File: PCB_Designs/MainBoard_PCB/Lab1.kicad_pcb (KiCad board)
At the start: 2 copper layers, 104.7 x 55.6 mm, 84 parts, among them K1 XLR3, P1 CONN_01X06, P10 CONN_01X01, P11 CONN_01X01, P12 CONN_01X01, P2 USB_B, P3 CONN_02X05, P4 CONN_01X02, P5 CONN_02X05, P6 CONN_02X05, P7 CONN_01X01, P8 CONN_01X01, P9 CONN_01X01, Q1 BSS138, Q2 BSS138, Q3 BSS138, Q4 BSS138, Q5 BSS138, Q6 BSS138, Q7 BSS138, U1 STM32F411RETx, U10 24C16, U2 TRACO_POWER_TEL_2-0511, U3 6N137, U4 6N137, U5 6N137, U6 FT232RL, U7 MAX481CSA, U8 UA78M05IDCY, U9 UA78M33CDCY, Y1 8MHz

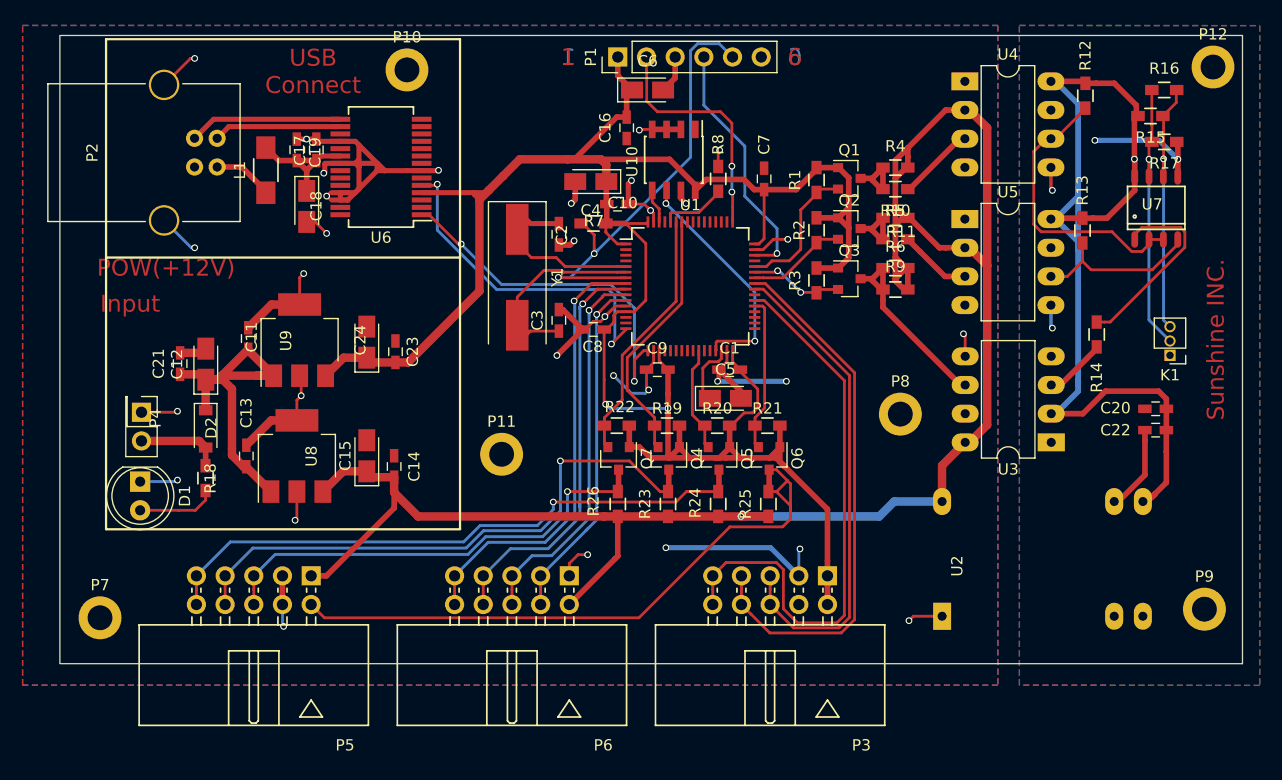
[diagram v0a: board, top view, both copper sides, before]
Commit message: Edited Main_PCB from feedback.
* Added RC-filter (1Mohm, 100nF)
Little cramped now, but whatever.
* Filled out groundplanes a little
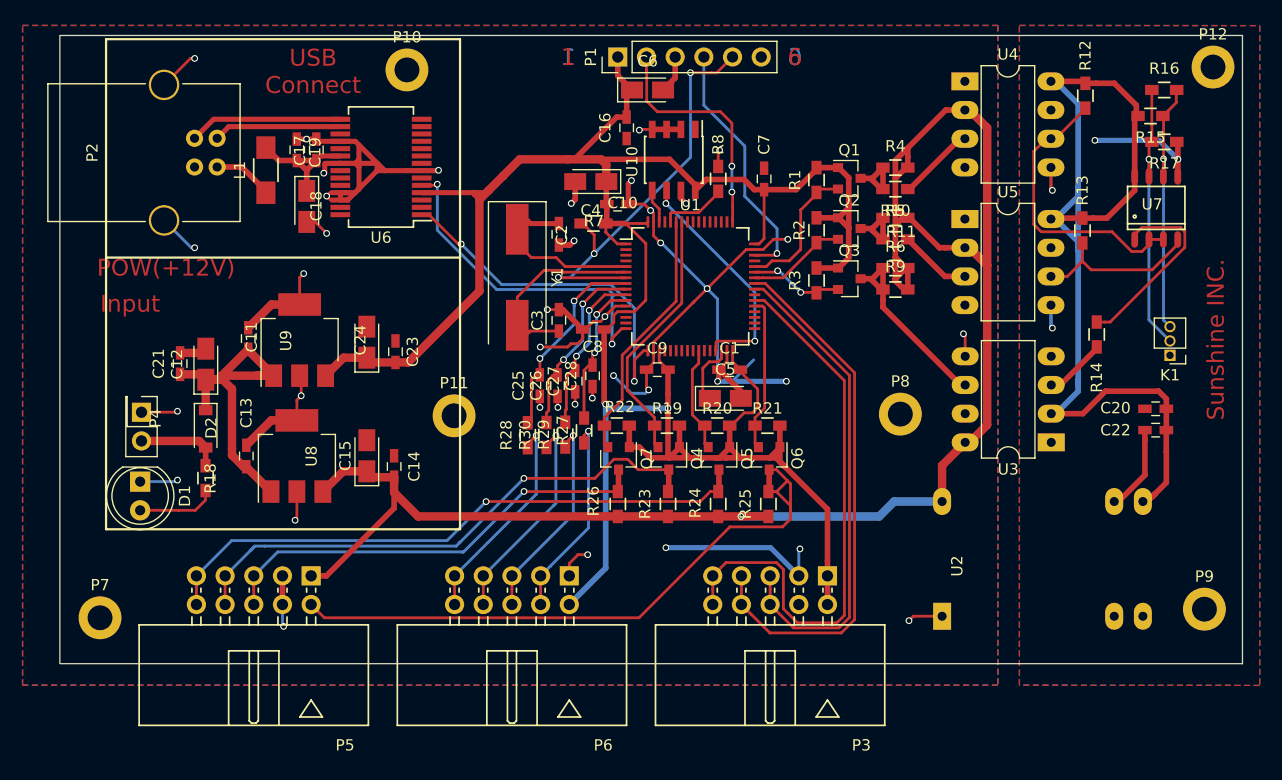
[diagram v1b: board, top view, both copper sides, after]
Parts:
- added C25: 100n, Capacitors_SMD:C_0603_HandSoldering, F.Cu at (77.5, 75.7)
- added C26: 100n, Capacitors_SMD:C_0603_HandSoldering, F.Cu at (79.1, 75.7)
- added C27: 100n, Capacitors_SMD:C_0603_HandSoldering, F.Cu at (80.7, 75.3)
- added C28: 100n, Capacitors_SMD:C_0603_HandSoldering, F.Cu at (82.2, 74.8)
- added R27: 1MEG, Resistors_SMD:R_0603_HandSoldering, F.Cu at (81.5, 79.7)
- added R28: 1MEG, Resistors_SMD:R_0603_HandSoldering, F.Cu at (76.5, 80.1)
- added R29: 1MEG, Resistors_SMD:R_0603_HandSoldering, F.Cu at (79.8, 80.0)
- added R30: 1MEG, Resistors_SMD:R_0603_HandSoldering, F.Cu at (78.1, 80.1)
- moved P11 5.41 mm to (70.0, 78.4)
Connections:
- P1 pad 6: (no net) -> Net-(P1-Pad6)
- P10 pad 1: (no net) -> Net-(P10-Pad1)
- P11 pad 1: (no net) -> Net-(P11-Pad1)
- P12 pad 1: (no net) -> Net-(P12-Pad1)
- P6 pad 2: +5V -> +3V3
- P7 pad 1: (no net) -> Net-(P7-Pad1)
- P8 pad 1: (no net) -> Net-(P8-Pad1)
- P9 pad 1: (no net) -> Net-(P9-Pad1)
- U1 pad 10: Net-(P6-Pad5) -> Net-(C27-Pad2)
- U1 pad 11: Net-(P6-Pad3) -> Net-(C28-Pad2)
- U1 pad 14: (no net) -> Net-(U1-Pad14)
- U1 pad 15: (no net) -> Net-(U1-Pad15)
- U1 pad 2: (no net) -> Net-(U1-Pad2)
- U1 pad 20: (no net) -> Net-(U1-Pad20)
- U1 pad 21: (no net) -> Net-(U1-Pad21)
- U1 pad 22: (no net) -> Net-(U1-Pad22)
- U1 pad 23: (no net) -> Net-(U1-Pad23)
- U1 pad 24: (no net) -> Net-(U1-Pad24)
- U1 pad 25: (no net) -> Net-(U1-Pad25)
- U1 pad 27: (no net) -> Net-(U1-Pad27)
- U1 pad 28: (no net) -> Net-(U1-Pad28)
- U1 pad 3: (no net) -> Net-(U1-Pad3)
- U1 pad 33: (no net) -> Net-(U1-Pad33)
- U1 pad 34: (no net) -> Net-(U1-Pad34)
- U1 pad 35: (no net) -> Net-(U1-Pad35)
- U1 pad 36: (no net) -> Net-(U1-Pad36)
- U1 pad 39: (no net) -> Net-(U1-Pad39)
- U1 pad 4: (no net) -> Net-(U1-Pad4)
- U1 pad 45: (no net) -> Net-(U1-Pad45)
- U1 pad 50: (no net) -> Net-(U1-Pad50)
- U1 pad 51: (no net) -> Net-(U1-Pad51)
- U1 pad 52: (no net) -> Net-(U1-Pad52)
- U1 pad 53: (no net) -> Net-(U1-Pad53)
- U1 pad 54: (no net) -> Net-(U1-Pad54)
- U1 pad 55: (no net) -> Net-(U1-Pad55)
- U1 pad 56: (no net) -> Net-(U1-Pad56)
- U1 pad 57: (no net) -> Net-(U1-Pad57)
- U1 pad 61: (no net) -> Net-(U1-Pad61)
- U1 pad 8: Net-(P6-Pad10) -> Net-(C25-Pad2)
- U1 pad 9: Net-(P6-Pad7) -> Net-(C26-Pad2)
- U10 pad 1: (no net) -> Net-(U10-Pad1)
- U2 pad 7: (no net) -> Net-(U2-Pad7)
- U2 pad 8: (no net) -> Net-(U2-Pad8)
- U3 pad 7: (no net) -> Net-(U3-Pad7)
- U4 pad 7: (no net) -> Net-(U4-Pad7)
- U5 pad 7: (no net) -> Net-(U5-Pad7)
- U6 pad 10: (no net) -> Net-(U6-Pad10)
- U6 pad 11: (no net) -> Net-(U6-Pad11)
- U6 pad 12: (no net) -> Net-(U6-Pad12)
- U6 pad 13: (no net) -> Net-(U6-Pad13)
- U6 pad 14: (no net) -> Net-(U6-Pad14)
- U6 pad 17: (no net) -> Net-(U6-Pad17)
- U6 pad 19: (no net) -> Net-(U6-Pad19)
- U6 pad 2: (no net) -> Net-(U6-Pad2)
- U6 pad 22: (no net) -> Net-(U6-Pad22)
- U6 pad 23: (no net) -> Net-(U6-Pad23)
- U6 pad 27: (no net) -> Net-(U6-Pad27)
- U6 pad 28: (no net) -> Net-(U6-Pad28)
- U6 pad 3: (no net) -> Net-(U6-Pad3)
- U6 pad 6: (no net) -> Net-(U6-Pad6)
- U6 pad 9: (no net) -> Net-(U6-Pad9)
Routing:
- net GND: track 158.9 -> 199.6 mm, vias 32 -> 39
- net Net-(P6-Pad10): track 39.7 -> 19.4 mm
- net +3V3: track 206.1 -> 225.2 mm
- net Net-(C25-Pad2): track 0.00 -> 18.2 mm, vias 0 -> 2
- net Net-(P6-Pad7): track 37.0 -> 19.0 mm
- net Net-(C26-Pad2): track 0.00 -> 16.6 mm, vias 0 -> 2
- net Net-(C27-Pad2): track 0.00 -> 15.2 mm, vias 0 -> 2
- net Net-(P6-Pad5): track 33.7 -> 18.6 mm
- net Net-(C28-Pad2): track 0.00 -> 13.1 mm, vias 0 -> 2
- net Net-(P6-Pad3): track 31.2 -> 18.7 mm
- net +5V: track 161.0 -> 151.4 mm
- net Net-(P5-Pad7): track 51.8 -> 48.9 mm
- net /NRST: track 39.3 -> 37.2 mm, vias 2 -> 3
- net Net-(P5-Pad5): track 40.9 -> 39.8 mm
- net /VDD5EXT: track 89.2 -> 89.5 mm, vias 1 -> 0

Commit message: Added pullups for EEPROM and button I/Os
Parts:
- added R31: 10K, Resistors_SMD:R_0603_HandSoldering, F.Cu at (103.3, 69.3)
- added R32: 10K, Resistors_SMD:R_0603_HandSoldering, F.Cu at (103.3, 71.2)
- added R33: 10K, Resistors_SMD:R_0603_HandSoldering, F.Cu at (88.8, 55.8)
- added R34: 10K, Resistors_SMD:R_0603_HandSoldering, F.Cu at (86.9, 55.8)
- moved U10 11.5 mm to (78.8, 51.3), turned to 0 degrees
- moved C7 4.89 mm to (99.6, 61.8), turned to 90 degrees
- moved C16 2.60 mm to (87.8, 52.6), turned to 180 degrees
- moved R8 2.16 mm to (91.9, 55.8)
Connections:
- U10 pad 1: Net-(U10-Pad1) -> GND
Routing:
- net +3V3: track 225.2 -> 307.1 mm, vias 2 -> 5
- net /EEPROM_I2C_SCL: track 20.9 -> 31.9 mm
- net /EEPROM_I2C_SDA: track 3.05 -> 12.2 mm
- net GND: track 199.6 -> 202.8 mm, vias 39 -> 36
- net /SWCLK: track 21.0 -> 19.1 mm, vias 2 -> 0
- net /BUTT_I2C_SCL: track 48.1 -> 49.3 mm
